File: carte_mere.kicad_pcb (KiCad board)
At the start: 4 copper layers, 85 x 85 mm, 235 parts, among them J1 Conn_01x02_Pin, J10 Conn_01x02_Pin, J11 Conn_01x02_Pin, J12 Conn_01x02_Pin, J13 Conn_01x02_Pin, J14 Conn_01x02, J15 Conn_01x04, J16 Conn_01x03_Pin, J17 Conn_01x05_Pin, J18 Conn_01x05_Pin, J19 Conn_01x05_Pin, J2 Conn_01x03_Pin, J20 Conn_01x04, J21 Conn_01x04, J22 Conn_01x04, J23 Conn_01x02, J25 Conn_01x02_Pin, J26 Conn_01x02_Pin, J27 Conn_01x02_Pin, J28 Conn_01x02_Pin, J29 Conn_01x02_Pin, J3 Conn_01x03_Pin, J30 Conn_01x02_Pin, J31 Conn_01x03_Pin, J32 Conn_01x03_Pin, J33 Conn_01x03_Pin, J34 Conn_01x03_Pin, J35 Conn_01x03_Pin, J36 Conn_01x03_Pin, J37 Conn_01x03_Pin, J38 Conn_01x03_Pin, J4 Conn_01x03_Pin, J5 Conn_01x03_Pin, J6 Conn_01x03_Pin, J7 Conn_01x03_Pin, J8 Conn_01x03_Pin, J9 Conn_01x03_Pin, Q1 MMBT3906, Q10 2N7002, Q11 MMBT3906, Q12 AO3401A, Q13 2N7002, Q14 MMBT3906, Q15 AO3401A, Q16 2N7002, Q17 MMBT3906, Q18 AO3401A, Q19 2N7002, Q2 2N7002, Q20 2N7002, Q21 2N7002, Q22 2N7002, Q23 2N7002, Q24 2N7002, Q25 2N7002, Q26 2N7002, Q27 2N7002, Q28 2N7002, Q29 2N7002, Q3 AO3401A, Q30 2N7002, Q31 2N7002, Q32 2N7002, Q33 2N7002, Q34 2N7002, Q35 2N7002, Q36 2N7002, Q37 2N7002, Q38 2N7002, Q39 2N7002, Q4 2N7002, Q40 2N7002, Q5 MMBT3906, Q6 AO3401A, Q7 2N7002, Q8 MMBT3906, Q9 AO3401A, U1 SN65HVD230, U2 SN74LVC1T45DBV, U5 TPS54302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

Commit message: clean
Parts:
- added J24: Conn_01x02, Connector_Molex:Molex_KK-254_AE-6410-02A_1x02_P2.54mm_Vertical, F.Cu at (149.7, 109.3)
- added R126: 100R, Capacitor_SMD:C_0402_1005Metric, F.Cu at (153.9, 50.3)
- added R127: 100R, Capacitor_SMD:C_0402_1005Metric, F.Cu at (153.9, 52.8)
- added R128: 100R, Capacitor_SMD:C_0402_1005Metric, F.Cu at (153.9, 57.9)
- added R129: 100R, Capacitor_SMD:C_0402_1005Metric, F.Cu at (152.1, 62.3)
- added R130: 100R, Capacitor_SMD:C_0402_1005Metric, F.Cu at (149.5, 62.3)
- added R131: 100R, Capacitor_SMD:C_0402_1005Metric, F.Cu at (146.6, 52.8)
- added R132: 100R, Capacitor_SMD:C_0402_1005Metric, F.Cu at (146.7, 57.9)
- added R133: 100R, Capacitor_SMD:C_0402_1005Metric, F.Cu at (149.5, 47.5)
- added R134: 100R, Capacitor_SMD:C_0402_1005Metric, F.Cu at (154.0, 69.3)
- added R135: 100R, Capacitor_SMD:C_0402_1005Metric, F.Cu at (153.9, 71.8)
- added R136: 100R, Capacitor_SMD:C_0402_1005Metric, F.Cu at (153.9, 76.9)
- added R137: 100R, Capacitor_SMD:C_0402_1005Metric, F.Cu at (152.2, 81.3)
- added R138: 100R, Capacitor_SMD:C_0402_1005Metric, F.Cu at (149.5, 66.4)
- added R139: 100R, Capacitor_SMD:C_0402_1005Metric, F.Cu at (146.7, 71.8)
- added R140: 100R, Capacitor_SMD:C_0402_1005Metric, F.Cu at (146.7, 76.9)
- added R141: 100R, Capacitor_SMD:C_0402_1005Metric, F.Cu at (149.6, 81.3)
- added R142: 100R, Capacitor_SMD:C_0402_1005Metric, F.Cu at (153.9, 87.8)
- added R143: 100R, Capacitor_SMD:C_0402_1005Metric, F.Cu at (153.9, 90.3)
- added R144: 100R, Capacitor_SMD:C_0402_1005Metric, F.Cu at (154.0, 96.5)
- added R145: 100R, Capacitor_SMD:C_0402_1005Metric, F.Cu at (152.0, 100.8)
- added R146: 100R, Capacitor_SMD:C_0402_1005Metric, F.Cu at (149.4, 85.8)
- added R147: 100R, Capacitor_SMD:C_0402_1005Metric, F.Cu at (146.4, 90.3)
- added R148: 100R, Capacitor_SMD:C_0402_1005Metric, F.Cu at (146.6, 95.4)
- added R149: 100R, Capacitor_SMD:C_0402_1005Metric, F.Cu at (149.4, 100.8)
- added R150: 100R, Capacitor_SMD:C_0402_1005Metric, F.Cu at (153.7, 109.2)
- added R151: 1k, Capacitor_SMD:C_0402_1005Metric, F.Cu at (150.1, 111.7)
- added R152: 2k, Capacitor_SMD:C_0402_1005Metric, F.Cu at (153.7, 107.2)
- added SPARE_1: Conn_02x05_Odd_Even, Connector_PinSocket_2.54mm:PinSocket_2x05_P2.54mm_Vertical, F.Cu at (151.6, 49.8)
- added SPARE_2: Conn_02x05_Odd_Even, Connector_PinSocket_2.54mm:PinSocket_2x05_P2.54mm_Vertical, F.Cu at (151.6, 68.8)
- added SPARE_3: Conn_02x05_Odd_Even, Connector_PinSocket_2.54mm:PinSocket_2x05_P2.54mm_Vertical, F.Cu at (151.5, 88.3)
- moved R125 1.22 mm to (209.9, 107.5)
- moved R123 1.17 mm to (211.8, 107.5)
- moved J23 0.92 mm to (210.9, 111.5)
- moved R124 0.92 mm to (213.2, 111.1)
- moved J13 0.30 mm to (229.1, 101.7)
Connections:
- JP1 pad JP1_10: unconnected-(JP1-Y19-PadJP1_10) -> spare3_5
- JP1 pad JP1_13: unconnected-(JP1-Y16-PadJP1_13) -> spare3_2
- JP1 pad JP1_14: unconnected-(JP1-Y17-PadJP1_14) -> spare3_1
- JP1 pad JP1_15: unconnected-(JP1-V17-PadJP1_15) -> spare3_6
- JP1 pad JP1_16: unconnected-(JP1-V18-PadJP1_16) -> spare3_4
- JP1 pad JP1_17: unconnected-(JP1-W14-PadJP1_17) -> spare2_6
- JP1 pad JP1_18: unconnected-(JP1-Y14-PadJP1_18) -> spare2_4
- JP1 pad JP1_19: unconnected-(JP1-V16-PadJP1_19) -> spare2_7
- JP1 pad JP1_20: unconnected-(JP1-W16-PadJP1_20) -> spare2_8
- JP1 pad JP1_21: unconnected-(JP1-T17-PadJP1_21) -> spare2_3
- JP1 pad JP1_22: unconnected-(JP1-R18-PadJP1_22) -> spare2_5
- JP1 pad JP1_23: unconnected-(JP1-V12-PadJP1_23) -> spare2_2
- JP1 pad JP1_24: unconnected-(JP1-W13-PadJP1_24) -> spare2_1
- JP1 pad JP1_25: unconnected-(JP1-T14-PadJP1_25) -> spare1_6
- JP1 pad JP1_26: unconnected-(JP1-T15-PadJP1_26) -> spare1_4
- JP1 pad JP1_27: unconnected-(JP1-T11-PadJP1_27) -> spare1_7
- JP1 pad JP1_28: unconnected-(JP1-T10-PadJP1_28) -> spare1_8
- JP1 pad JP1_31: unconnected-(JP1-V15-PadJP1_31) -> spare1_3
- JP1 pad JP1_32: unconnected-(JP1-W15-PadJP1_32) -> spare1_5
- JP1 pad JP1_33: unconnected-(JP1-P14-PadJP1_33) -> spare1_1
- JP1 pad JP1_34: unconnected-(JP1-R14-PadJP1_34) -> spare1_2
- JP1 pad JP1_6: unconnected-(JP1-U17-PadJP1_6) -> spare3_8
- JP1 pad JP1_8: unconnected-(JP1-W19-PadJP1_8) -> spare3_7
- JP1 pad JP1_9: unconnected-(JP1-Y18-PadJP1_9) -> spare3_3
- JP1 pad JP2_23: QEI_1_A -> QEI_3_X
- JP1 pad JP2_25: QEI_1_B -> QEI_3_A
- JP1 pad JP2_26: QEI_3_X -> QEI_3_B
- JP1 pad JP2_27: QEI_1_X -> QEI_2_B
- JP1 pad JP2_28: QEI_3_A -> QEI_2_A
- JP1 pad JP2_31: QEI_2_A -> Tirette
- JP1 pad JP2_32: QEI_3_B -> QEI_2_X
- JP1 pad JP2_33: QEI_2_B -> QEI_1_A
- JP1 pad JP2_34: AU -> QEI_1_B
- JP1 pad JP2_35: QEI_2_X -> QEI_1_X
- JP1 pad JP2_36: Tirette -> AU
- JP1 pad JP2_38: unconnected-(JP1-J19-PadJP2_38) -> TEAM
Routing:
- net TEAM: track 0.00 -> 69.5 mm, vias 0 -> 2
- net 3.3V: track 92.1 -> 44.5 mm
- net spare1_4: track 0.00 -> 28.1 mm, vias 0 -> 2
- net spare3_6: track 0.00 -> 25.3 mm, vias 0 -> 2
- net spare1_6: track 0.00 -> 24.6 mm
- net spare1_2: track 0.00 -> 21.2 mm, vias 0 -> 2
- net spare2_4: track 0.00 -> 21.0 mm, vias 0 -> 2
- net QEI_1_A: track 43.1 -> 23.1 mm, vias 1 -> 0
- net spare2_6: track 0.00 -> 17.9 mm
- net spare2_2: track 0.00 -> 17.6 mm
- net QEI_1_B: track 42.4 -> 24.9 mm, vias 1 -> 0
- net spare3_4: track 0.00 -> 16.7 mm
- net spare1_1: track 0.00 -> 16.6 mm
- net spare1_3: track 0.00 -> 16.5 mm
- net spare1_8: track 0.00 -> 13.7 mm
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- added copper zone on B.Cu, net GND
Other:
- board size 85 x 85 mm -> 87 x 85 mm
- board text added: "3.3V"
- board text added: "5V"
- board text added: "TEAM"

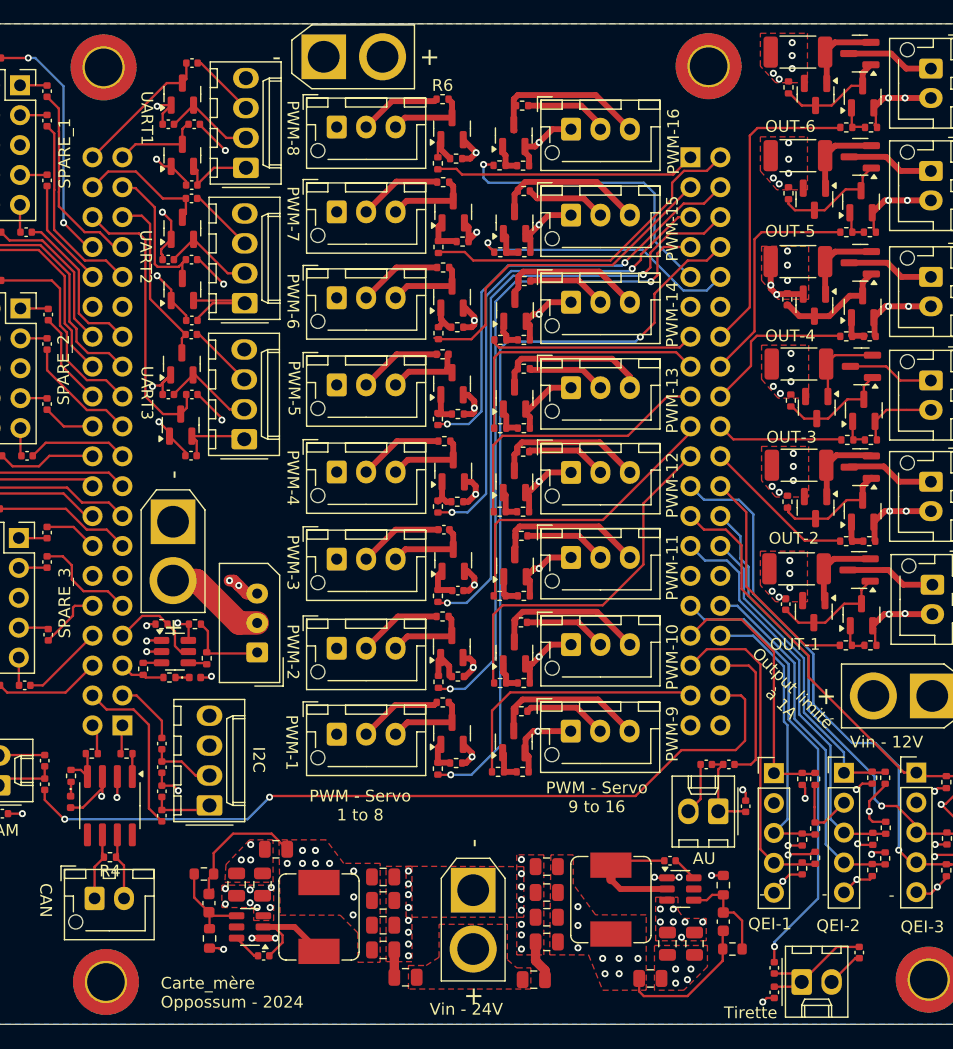
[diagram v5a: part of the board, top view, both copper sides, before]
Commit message: fix issue on zynq footprint
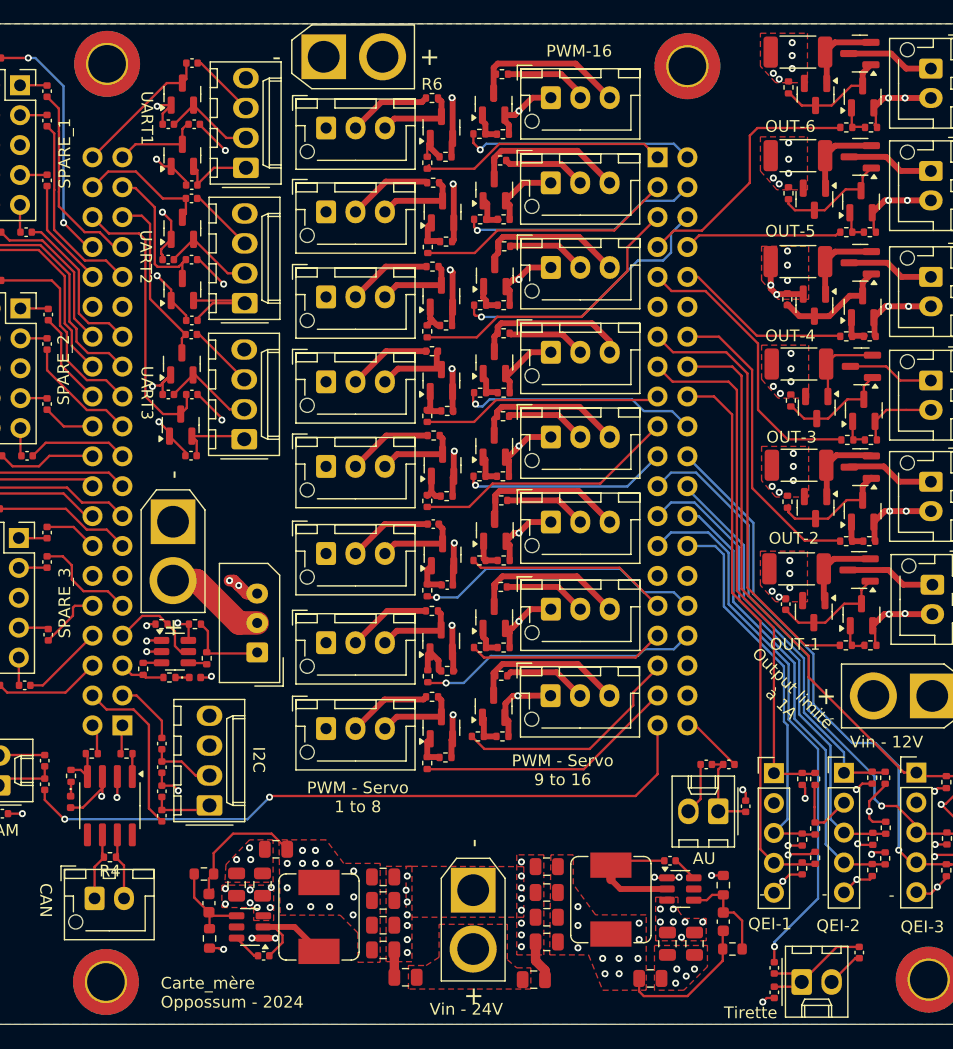
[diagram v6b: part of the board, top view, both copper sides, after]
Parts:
- moved J34 3.47 mm to (196.7, 72.5)
- moved J35 3.47 mm to (196.7, 79.7)
- moved J36 3.47 mm to (196.7, 86.9)
- moved J8 3.47 mm to (196.7, 94.3)
- moved Q28 3.47 mm to (191.9, 73.4)
- moved Q29 3.47 mm to (191.9, 80.5)
- moved Q30 3.47 mm to (191.9, 87.6)
- moved Q34 3.47 mm to (191.8, 102.6)
- moved R19 3.47 mm to (190.5, 105.1)
- moved R23 3.47 mm to (192.4, 92.4)
- moved R24 3.47 mm to (192.6, 105.1)
- moved R87 3.47 mm to (190.7, 75.9)
- moved R88 3.47 mm to (192.7, 75.9)
- moved R89 3.47 mm to (192.7, 70.9)
- moved R90 3.47 mm to (190.6, 83.0)
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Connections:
- JP1 pad JP2_10: SERVO10 -> DSO_6
- JP1 pad JP2_13: SERVO11 -> DSO_5
- JP1 pad JP2_14: DSO_1 -> DSO_4
- JP1 pad JP2_15: SERVO12 -> QEI_1_A
- JP1 pad JP2_16: DSO_2 -> QEI_3_A
- JP1 pad JP2_17: SERVO13 -> SERVO4
- JP1 pad JP2_18: DSO_6 -> QEI_1_X
- JP1 pad JP2_19: SERVO14 -> SERVO5
- JP1 pad JP2_2: SERVO2 -> SERVO9
- JP1 pad JP2_20: DSO_3 -> SERVO12
- JP1 pad JP2_21: SERVO15 -> SERVO13
- JP1 pad JP2_22: DSO_4 -> QEI_3_X
- JP1 pad JP2_23: QEI_3_X -> QEI_3_B
- JP1 pad JP2_24: DSO_5 -> QEI_2_A
- JP1 pad JP2_25: QEI_3_A -> QEI_2_B
- JP1 pad JP2_26: QEI_3_B -> QEI_2_X
- JP1 pad JP2_27: QEI_2_B -> Tirette
- JP1 pad JP2_28: QEI_2_A -> QEI_1_B
- JP1 pad JP2_3: SERVO3 -> SERVO2
- JP1 pad JP2_31: Tirette -> SERVO14
- JP1 pad JP2_32: QEI_2_X -> SERVO6
- JP1 pad JP2_33: QEI_1_A -> SERVO15
- JP1 pad JP2_34: QEI_1_B -> SERVO7
- JP1 pad JP2_35: QEI_1_X -> SERVO16
- JP1 pad JP2_36: AU -> unconnected-(JP1-M20-PadJP2_36)
- JP1 pad JP2_37: SERVO16 -> SERVO8
- JP1 pad JP2_38: TEAM -> unconnected-(JP1-J19-PadJP2_38)
- JP1 pad JP2_39: unconnected-(JP1-J20-PadJP2_39) -> TEAM
- JP1 pad JP2_4: SERVO4 -> SERVO10
- JP1 pad JP2_40: unconnected-(JP1-H20-PadJP2_40) -> AU
- JP1 pad JP2_5: SERVO5 -> SERVO3
- JP1 pad JP2_6: SERVO6 -> SERVO11
- JP1 pad JP2_7: SERVO7 -> DSO_1
- JP1 pad JP2_8: SERVO8 -> DSO_2
- JP1 pad JP2_9: SERVO9 -> DSO_3
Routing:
- net SERVO8: track 63.9 -> 22.3 mm, vias 2 -> 0
- net SERVO7: track 56.0 -> 24.0 mm, vias 2 -> 1
- net SERVO6: track 52.3 -> 24.4 mm, vias 2 -> 1
- net QEI_1_A: track 23.1 -> 45.5 mm
- net QEI_1_X: track 27.5 -> 47.1 mm
- net SERVO5: track 42.0 -> 22.5 mm, vias 2 -> 0
- net SERVO4: track 38.3 -> 20.5 mm, vias 2 -> 0
- net DSO_5: track 19.7 -> 37.3 mm
- net DSO_3: track 10.8 -> 25.5 mm
- net SERVO15: track 31.2 -> 16.8 mm
- net QEI_3_A: track 35.0 -> 48.9 mm
- net DSO_4: track 13.2 -> 26.1 mm
- net GND: track 163.2 -> 173.5 mm, vias 68 -> 66
- net TEAM: track 69.5 -> 59.3 mm
- net SERVO14: track 26.5 -> 17.4 mm
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- added copper zone on B.Cu, net SERVO6
- removed copper zone on B.Cu, net GND
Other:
- board text removed: "PWM-1"
- board text removed: "PWM-10"
- board text removed: "PWM-11"
- board text removed: "PWM-12"
- board text removed: "PWM-13"
- board text removed: "PWM-14"
- board text removed: "PWM-15"
- board text removed: "PWM-2"
- board text removed: "PWM-3"
- board text removed: "PWM-4"
- board text removed: "PWM-5"
- board text removed: "PWM-6"
- board text removed: "PWM-7"
- board text removed: "PWM-8"
- board text removed: "PWM-9"
